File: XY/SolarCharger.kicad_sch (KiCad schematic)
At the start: 42 parts, among them U13 ADM1176-1ARMZ-R7

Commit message: Updated layout
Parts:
- F6, F7, F8: footprint (none) -> Fuse:Fuse_0603_1608Metric
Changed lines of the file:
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@@
 			)
 		)
-		(property "Footprint" ""
+		(property "Footprint" "Fuse:Fuse_0603_1608Metric"
 			(at 41.91 153.67 0)
 			(effects
@@
 			)
 		)
-		(property "Footprint" ""
+		(property "Footprint" "Fuse:Fuse_0603_1608Metric"
 			(at 41.91 109.22 0)
 			(effects
@@
 			)
 		)
-		(property "Footprint" ""
+		(property "Footprint" "Fuse:Fuse_0603_1608Metric"
 			(at 123.19 31.75 0)
 			(effects

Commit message: almost done
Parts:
- added SC6: SM141K06TF, Argus-Miscellaneous:SM141K06TF, symbol Device:Solar_Cell
- SC1, SC2, SC4, SC5: footprint SolarPanels:SM141K06TF -> Argus-Miscellaneous:SM141K06TF
- SC3: footprint SolarPanels:SM141K10TF -> Argus-Miscellaneous:SM141K10TF
- U13: symbol Mainboard:ADM1176-1ARMZ-R7 -> Argus-IC:ADM1176-1ARMZ-R7
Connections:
- net at D3.1 (K), D4.2 (A), SC3.1 (+)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: now also SC6.1 (+)
- net at D2.1 (K), D3.2 (A), SC2.1 (+)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: now also SC6.2 (-)
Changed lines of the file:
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@@
 	(wire
 		(pts
+			(xy 90.17 39.37) (xy 92.71 39.37)
+		)
+		(stroke
+			(width 0)
+			(type default)
+		)
+	)
+	(wire
+		(pts
 			(xy 99.06 91.44) (xy 105.41 91.44)
 		)
@@
 	(wire
 		(pts
+			(xy 82.55 39.37) (xy 80.01 39.37)
+		)
+		(stroke
+			(width 0)
+			(type default)
+		)
+	)
+	(wire
+		(pts
 			(xy 105.41 168.91) (xy 111.76 168.91)
 		)
@@
 	(wire
 		(pts
+			(xy 80.01 39.37) (xy 80.01 31.75)
+		)
+		(stroke
+			(width 0)
+			(type default)
+		)
+	)
+	(wire
+		(pts
 			(xy 62.23 123.19) (xy 62.23 124.46)
 		)
@@
 	(wire
 		(pts
+			(xy 92.71 39.37) (xy 92.71 31.75)
+		)
+		(stroke
+			(width 0)
+			(type default)
+		)
+	)
+	(wire
+		(pts
 			(xy 212.09 81.28) (xy 217.17 81.28)
 		)
@@
 			)
 		)
-		(property "Footprint" "SolarPanels:SM141K06TF"
+		(property "Footprint" "Argus-Miscellaneous:SM141K06TF"
 			(at 99.314 31.75 90)
 			(effects
@@
 	)
 	(symbol
-		(lib_id "Mainboard:ADM1176-1ARMZ-R7")
+		(lib_id "Argus-IC:ADM1176-1ARMZ-R7")
 		(at 233.68 81.28 0)
 		(unit 1)
@@
 	)
 	(symbol
+		(lib_id "Device:Solar_Cell")
+		(at 85.09 39.37 270)
+		(unit 1)
+		(exclude_from_sim no)
+		(in_bom yes)
+		(on_board yes)
+		(dnp yes)
+		(property "Reference" "SC6"
+			(at 86.614 43.18 90)
+			(effects
+				(font
+					(size 1.27 1.27)
+				)
+			)
+		)
+		(property "Value" "SM141K06TF"
+			(at 86.868 45.212 90)
+			(effects
+				(font
+					(size 1.27 1.27)
+				)
+			)
+		)
+		(property "Footprint" "Argus-Miscellaneous:SM141K06TF"
+			(at 86.614 39.37 90)
+			(effects
+				(font
+					(size 1.27 1.27)
+				)
+				(hide yes)
+			)
+		)
+		(property "Datasheet" "~"
+			(at 86.614 39.37 90)
+			(effects
+				(font
+					(size 1.27 1.27)
+				)
+				(hide yes)
+			)
+		)
+		(property "Description" "Single solar cell"
+			(at 85.09 39.37 0)
+			(effects
+				(font
+					(size 1.27 1.27)
+				)
+				(hide yes)
+			)
+		)
+		(pin "2"
+		)
+		(pin "1"
+		)
+		(instances
+			(project "Avionics-SolarPanels"
+				(path "/92e58b76-9357-4452-b231-18fffdf58e73/bef00a2e-eb3a-4ecf-812a-1c3ccf6e8d66"
+					(reference "SC6")
+					(unit 1)
+				)
+			)
+		)
+	)
+	(symbol
 		(lib_id "Device:R_Small")
 		(at 111.76 68.58 0)
@@
 			)
 		)
-		(property "Footprint" "SolarPanels:SM141K06TF"
+		(property "Footprint" "Argus-Miscellaneous:SM141K06TF"
 			(at 112.014 31.75 90)
 			(effects
@@
 			)
 		)
-		(property "Footprint" "SolarPanels:SM141K06TF"
+		(property "Footprint" "Argus-Miscellaneous:SM141K06TF"
 			(at 61.214 31.75 90)
 			(effects
@@
 			)
 		)
-		(property "Footprint" "SolarPanels:SM141K06TF"
+		(property "Footprint" "Argus-Miscellaneous:SM141K06TF"
 			(at 73.914 31.75 90)
 			(effects
@@
 			)
 		)
-		(property "Footprint" "SolarPanels:SM141K10TF"
+		(property "Footprint" "Argus-Miscellaneous:SM141K10TF"
 			(at 86.614 31.75 90)
 			(effects

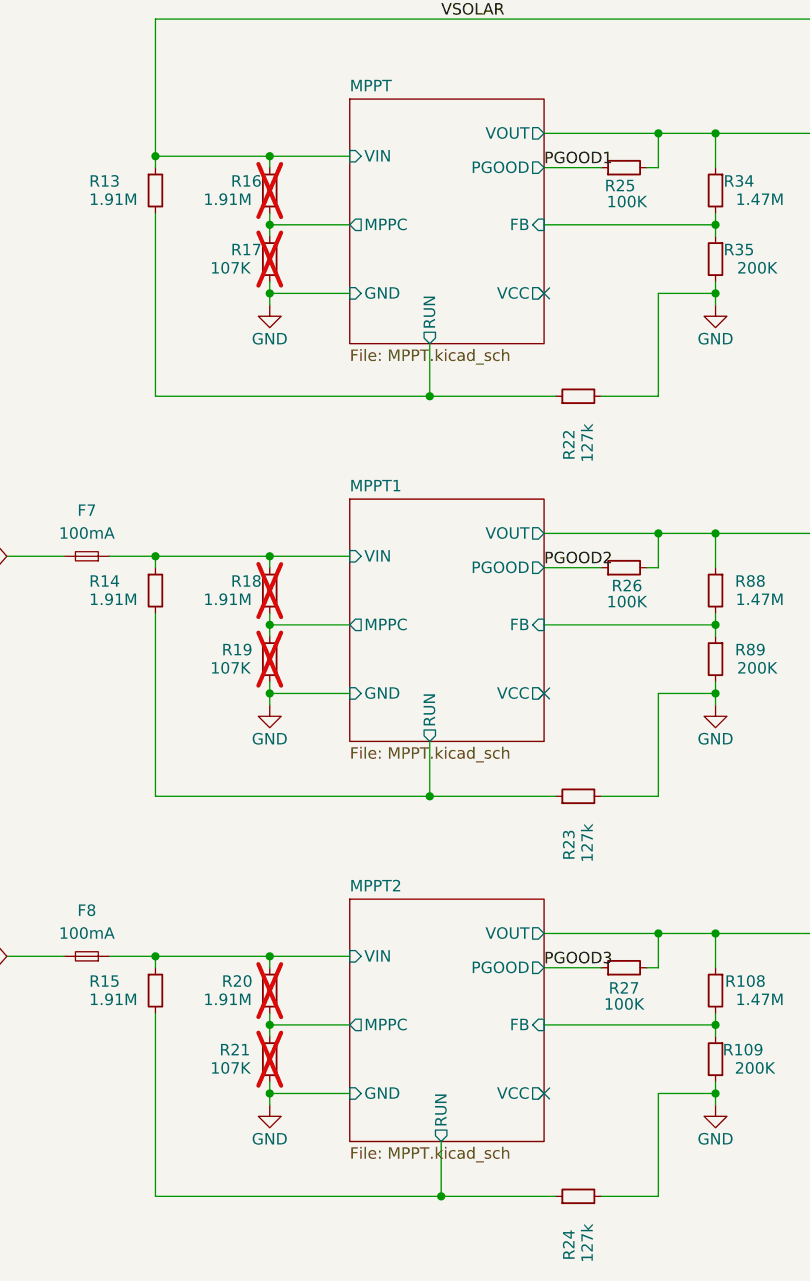
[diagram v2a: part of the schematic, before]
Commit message: Increased usbc connnector size
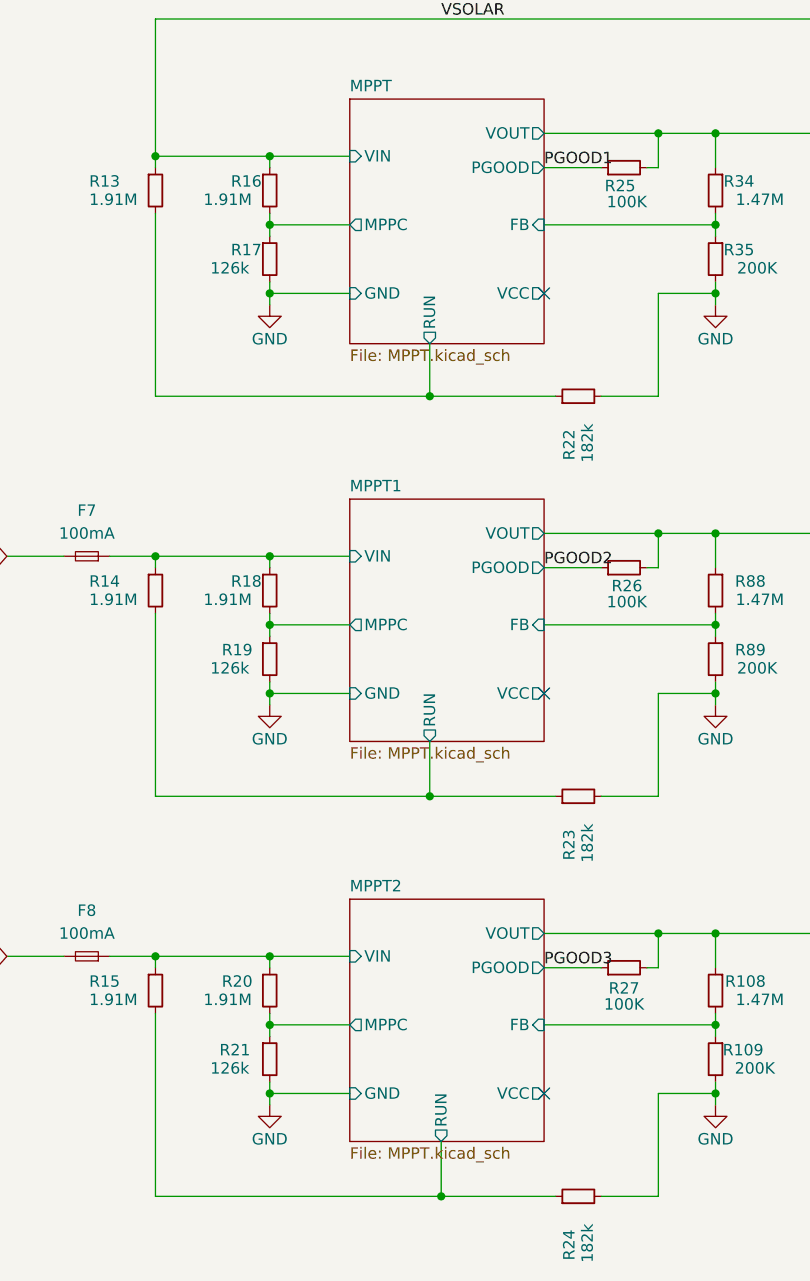
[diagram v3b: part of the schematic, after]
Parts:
- R16, R18, R20: now fitted
- R17, R19, R21: value 107K -> 126k; now fitted
- R22, R23, R24: value 127k -> 182k
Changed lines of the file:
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@@
 		(in_bom yes)
 		(on_board yes)
-		(dnp yes)
+		(dnp no)
 		(property "Reference" "R16"
 			(at 57.912 67.564 0)
@@
 		(in_bom yes)
 		(on_board yes)
-		(dnp yes)
+		(dnp no)
 		(property "Reference" "R20"
 			(at 56.896 156.464 0)
@@
 		(in_bom yes)
 		(on_board yes)
-		(dnp yes)
+		(dnp no)
 		(property "Reference" "R21"
 			(at 56.642 164.084 0)
@@
 			)
 		)
-		(property "Value" "107K"
+		(property "Value" "126k"
 			(at 55.626 166.116 0)
 			(effects
@@
 			)
 		)
-		(property "Value" "127k"
+		(property "Value" "182k"
 			(at 97.536 187.706 0)
 			(effects
@@
 			)
 		)
-		(property "Value" "127k"
+		(property "Value" "182k"
 			(at 97.536 98.806 0)
 			(effects
@@
 		(in_bom yes)
 		(on_board yes)
-		(dnp yes)
+		(dnp no)
 		(property "Reference" "R18"
 			(at 57.912 112.014 0)
@@
 		(in_bom yes)
 		(on_board yes)
-		(dnp yes)
+		(dnp no)
 		(property "Reference" "R19"
 			(at 56.896 119.634 0)
@@
 			)
 		)
-		(property "Value" "107K"
+		(property "Value" "126k"
 			(at 55.626 121.666 0)
 			(effects
@@
 			)
 		)
-		(property "Value" "127k"
+		(property "Value" "182k"
 			(at 97.536 143.256 0)
 			(effects
@@
 		(in_bom yes)
 		(on_board yes)
-		(dnp yes)
+		(dnp no)
 		(property "Reference" "R17"
 			(at 57.912 75.184 0)
@@
 			)
 		)
-		(property "Value" "107K"
+		(property "Value" "126k"
 			(at 55.626 77.216 0)
 			(effects

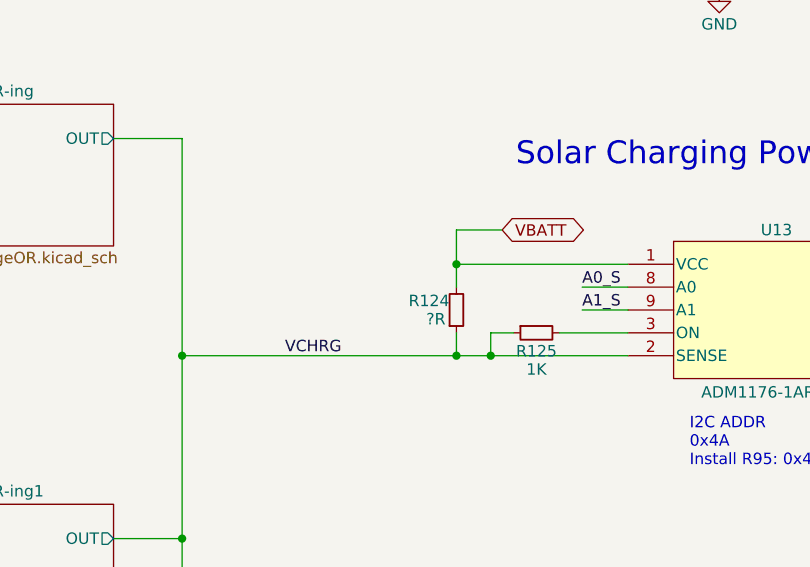
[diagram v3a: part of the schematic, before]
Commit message: Added fusing to power monitor
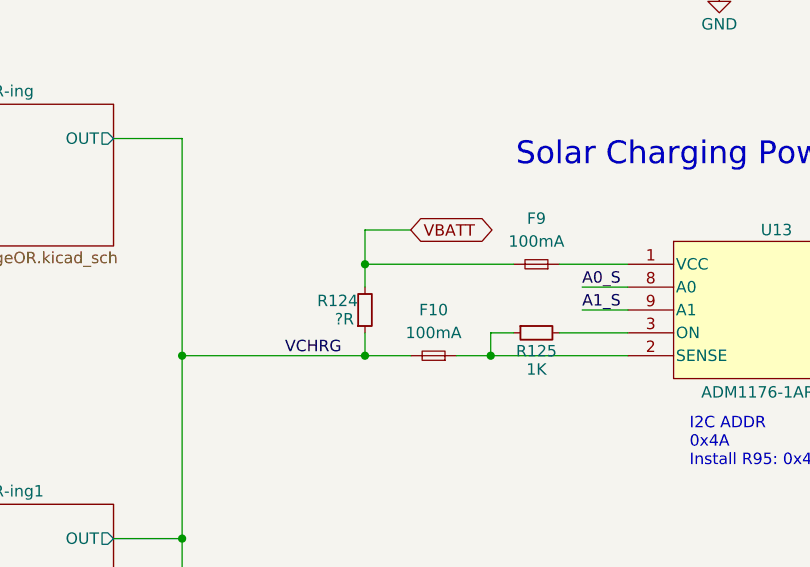
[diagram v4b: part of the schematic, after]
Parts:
- added F10, F9: 100mA, Fuse:Fuse_0603_1608Metric, symbol Device:Fuse_Small
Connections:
- net VBATT: now also F9.2; no longer U13.1 (VCC)
- net VCHRG: now also F10.2; no longer R125.1, U13.2 (SENSE)
- new net: F9.1, U13.1 (VCC)
- new net: F10.1, R125.1, U13.2 (SENSE)
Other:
- moved on the sheet: R124
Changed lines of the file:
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@@
 	)
 	(junction
-		(at 198.12 76.2)
-		(diameter 0)
-		(color 0 0 0 0)
-	)
-	(junction
 		(at 111.76 168.91)
 		(diameter 0)
@@
 	)
 	(junction
+		(at 201.93 86.36)
+		(diameter 0)
+		(color 0 0 0 0)
+	)
+	(junction
 		(at 227.33 35.56)
 		(diameter 0)
@@
 	)
 	(junction
+		(at 187.96 76.2)
+		(diameter 0)
+		(color 0 0 0 0)
+	)
+	(junction
 		(at 80.01 31.75)
 		(diameter 0)
@@
 	)
 	(junction
-		(at 198.12 86.36)
-		(diameter 0)
-		(color 0 0 0 0)
-	)
-	(junction
 		(at 67.31 31.75)
 		(diameter 0)
@@
 	)
 	(junction
-		(at 201.93 86.36)
-		(diameter 0)
-		(color 0 0 0 0)
-	)
-	(junction
 		(at 62.23 80.01)
 		(diameter 0)
@@
 	)
 	(junction
+		(at 187.96 86.36)
+		(diameter 0)
+		(color 0 0 0 0)
+	)
+	(junction
 		(at 105.41 31.75)
 		(diameter 0)
@@
 	(wire
 		(pts
-			(xy 198.12 76.2) (xy 198.12 72.39)
+			(xy 187.96 72.39) (xy 187.96 76.2)
 		)
 		(stroke
@@
 	(wire
 		(pts
-			(xy 114.3 25.4) (xy 118.11 25.4)
+			(xy 187.96 76.2) (xy 204.47 76.2)
 		)
 		(stroke
@@
 	(wire
 		(pts
-			(xy 242.57 146.05) (xy 261.62 146.05)
+			(xy 114.3 25.4) (xy 118.11 25.4)
 		)
 		(stroke
@@
 	(wire
 		(pts
-			(xy 198.12 76.2) (xy 198.12 78.74)
+			(xy 242.57 146.05) (xy 261.62 146.05)
 		)
 		(stroke
@@
 	(wire
 		(pts
+			(xy 187.96 86.36) (xy 193.04 86.36)
+		)
+		(stroke
+			(width 0)
+			(type default)
+		)
+	)
+	(wire
+		(pts
 			(xy 49.53 153.67) (xy 49.53 154.94)
 		)
@@
 	(wire
 		(pts
-			(xy 105.41 151.13) (xy 105.41 154.94)
+			(xy 187.96 76.2) (xy 187.96 78.74)
 		)
 		(stroke
@@
 	(wire
 		(pts
-			(xy 80.01 31.75) (xy 80.01 25.4)
+			(xy 105.41 151.13) (xy 105.41 154.94)
 		)
 		(stroke
@@
 	(wire
 		(pts
-			(xy 242.57 35.56) (xy 245.11 35.56)
+			(xy 80.01 31.75) (xy 80.01 25.4)
 		)
 		(stroke
@@
 	(wire
 		(pts
-			(xy 99.06 135.89) (xy 105.41 135.89)
+			(xy 242.57 35.56) (xy 245.11 35.56)
 		)
 		(stroke
@@
 	(wire
 		(pts
-			(xy 82.55 39.37) (xy 80.01 39.37)
+			(xy 99.06 135.89) (xy 105.41 135.89)
 		)
 		(stroke
@@
 	(wire
 		(pts
-			(xy 105.41 168.91) (xy 111.76 168.91)
+			(xy 82.55 39.37) (xy 80.01 39.37)
 		)
 		(stroke
@@
 	(wire
 		(pts
-			(xy 198.12 86.36) (xy 201.93 86.36)
+			(xy 105.41 168.91) (xy 111.76 168.91)
 		)
 		(stroke
@@
 	(wire
 		(pts
-			(xy 203.2 72.39) (xy 198.12 72.39)
+			(xy 193.04 72.39) (xy 187.96 72.39)
 		)
 		(stroke
@@
 	(wire
 		(pts
-			(xy 167.64 86.36) (xy 198.12 86.36)
+			(xy 167.64 86.36) (xy 187.96 86.36)
 		)
 		(stroke
@@
 	(wire
 		(pts
+			(xy 209.55 76.2) (xy 217.17 76.2)
+		)
+		(stroke
+			(width 0)
+			(type default)
+		)
+	)
+	(wire
+		(pts
 			(xy 67.31 25.4) (xy 71.12 25.4)
 		)
@@
 	(wire
 		(pts
-			(xy 198.12 83.82) (xy 198.12 86.36)
+			(xy 187.96 83.82) (xy 187.96 86.36)
+		)
+		(stroke
+			(width 0)
+			(type default)
+		)
+	)
+	(wire
+		(pts
+			(xy 198.12 86.36) (xy 201.93 86.36)
 		)
 		(stroke
@@
 	(wire
 		(pts
-			(xy 198.12 76.2) (xy 217.17 76.2)
-		)
-		(stroke
-			(width 0)
-			(type default)
-		)
-	)
-	(wire
-		(pts
 			(xy 111.76 168.91) (xy 111.76 170.18)
 		)
@@
 	(global_label "VBATT"
 		(shape bidirectional)
-		(at 203.2 72.39 0)
+		(at 193.04 72.39 0)
 		(effects
 			(font
@@
 		)
 		(property "Intersheetrefs" "${INTERSHEET_REFS}"
-			(at 203.2 72.39 0)
+			(at 193.04 72.39 0)
 			(effects
 				(font
@@
 	)
 	(symbol
+		(lib_id "Device:Fuse_Small")
+		(at 207.01 76.2 180)
+		(unit 1)
+		(exclude_from_sim no)
+		(in_bom yes)
+		(on_board yes)
+		(dnp no)
+		(fields_autoplaced yes)
+		(property "Reference" "F9"
+			(at 207.01 71.12 0)
+			(effects
+				(font
+					(size 1.27 1.27)
+				)
+			)
+		)
+		(property "Value" "100mA"
+			(at 207.01 73.66 0)
+			(effects
+				(font
+					(size 1.27 1.27)
+				)
+			)
+		)
+		(property "Footprint" "Fuse:Fuse_0603_1608Metric"
+			(at 207.01 76.2 0)
+			(effects
+				(font
+					(size 1.27 1.27)
+				)
+				(hide yes)
+			)
+		)
+		(property "Datasheet" "~"
+			(at 207.01 76.2 0)
+			(effects
+				(font
+					(size 1.27 1.27)
+				)
+				(hide yes)
+			)
+		)
+		(property "Description" "Fuse, small symbol"
+			(at 207.01 76.2 0)
+			(effects
+				(font
+					(size 1.27 1.27)
+				)
+				(hide yes)
+			)
+		)
+		(pin "2"
+		)
+		(pin "1"
+		)
+		(instances
+			(project "Avionics-SolarPanels"
+				(path "/92e58b76-9357-4452-b231-18fffdf58e73/bef00a2e-eb3a-4ecf-812a-1c3ccf6e8d66"
+					(reference "F9")
+					(unit 1)
+				)
+			)
+		)
+	)
+	(symbol
 		(lib_id "Device:C_Small")
 		(at 260.35 76.2 270)
@@
 	)
 	(symbol
+		(lib_id "Device:Fuse_Small")
+		(at 195.58 86.36 180)
+		(unit 1)
+		(exclude_from_sim no)
+		(in_bom yes)
+		(on_board yes)
+		(dnp no)
+		(fields_autoplaced yes)
+		(property "Reference" "F10"
+			(at 195.58 81.28 0)
+			(effects
+				(font
+					(size 1.27 1.27)
+				)
+			)
+		)
+		(property "Value" "100mA"
+			(at 195.58 83.82 0)
+			(effects
+				(font
+					(size 1.27 1.27)
+				)
+			)
+		)
+		(property "Footprint" "Fuse:Fuse_0603_1608Metric"
+			(at 195.58 86.36 0)
+			(effects
+				(font
+					(size 1.27 1.27)
+				)
+				(hide yes)
+			)
+		)
+		(property "Datasheet" "~"
+			(at 195.58 86.36 0)
+			(effects
+				(font
+					(size 1.27 1.27)
+				)
+				(hide yes)
+			)
+		)
+		(property "Description" "Fuse, small symbol"
+			(at 195.58 86.36 0)
+			(effects
+				(font
+					(size 1.27 1.27)
+				)
+				(hide yes)
+			)
+		)
+		(pin "2"
+		)
+		(pin "1"
+		)
+		(instances
+			(project "Avionics-SolarPanels"
+				(path "/92e58b76-9357-4452-b231-18fffdf58e73/bef00a2e-eb3a-4ecf-812a-1c3ccf6e8d66"
+					(reference "F10")
+					(unit 1)
+				)
+			)
+		)
+	)
+	(symbol
 		(lib_id "Device:R_Small")
 		(at 111.76 165.1 0)
@@
 	(symbol
 		(lib_id "Device:R_Small")
-		(at 198.12 81.28 0)
+		(at 187.96 81.28 0)
 		(mirror x)
 		(unit 1)
@@
 		(dnp no)
 		(property "Reference" "R124"
-			(at 195.072 80.264 0)
+			(at 184.912 80.264 0)
 			(effects
 				(font
@@
 		)
 		(property "Value" "?R"
-			(at 195.834 82.296 0)
+			(at 185.674 82.296 0)
 			(effects
 				(font
@@
 		)
 		(property "Footprint" "Resistor_SMD:R_2512_6332Metric"
-			(at 198.12 81.28 0)
+			(at 187.96 81.28 0)
 			(effects
 				(font
@@
 		)
 		(property "Datasheet" "~"
-			(at 198.12 81.28 0)
+			(at 187.96 81.28 0)
 			(effects
 				(font
@@
 		)
 		(property "Description" "Resistor, small symbol"
-			(at 198.12 81.28 0)
+			(at 187.96 81.28 0)
 			(effects
 				(font

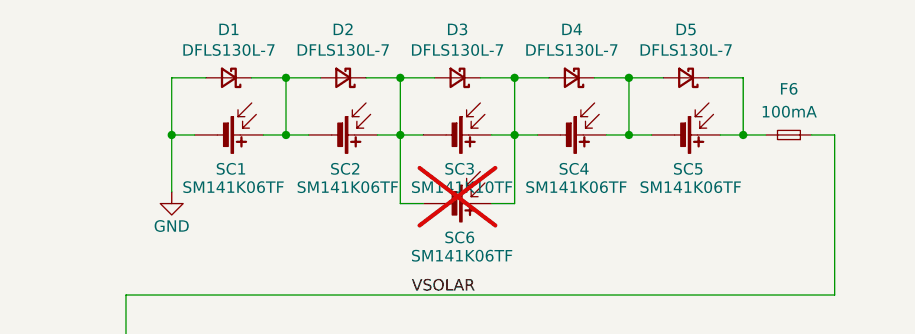
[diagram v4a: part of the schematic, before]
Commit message: Updated silkscreen and part number for solar panel bypass
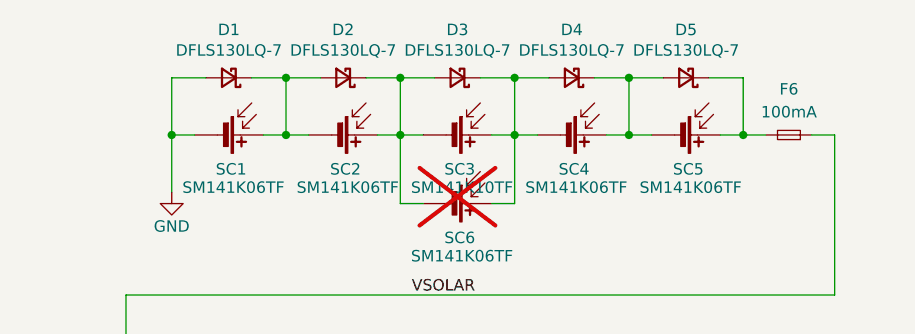
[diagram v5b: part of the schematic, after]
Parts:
- D1, D2, D3, D4, D5: value DFLS130L-7 -> DFLS130LQ-7
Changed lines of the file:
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@@
 			)
 		)
-		(property "Value" "DFLS130L-7"
+		(property "Value" "DFLS130LQ-7"
 			(at 86.36 22.352 0)
 			(effects
@@
 			)
 		)
-		(property "Value" "DFLS130L-7"
+		(property "Value" "DFLS130LQ-7"
 			(at 73.66 22.352 0)
 			(effects
@@
 			)
 		)
-		(property "Value" "DFLS130L-7"
+		(property "Value" "DFLS130LQ-7"
 			(at 99.06 22.352 0)
 			(effects
@@
 			)
 		)
-		(property "Value" "DFLS130L-7"
+		(property "Value" "DFLS130LQ-7"
 			(at 60.96 22.352 0)
 			(effects
@@
 			)
 		)
-		(property "Value" "DFLS130L-7"
+		(property "Value" "DFLS130LQ-7"
 			(at 111.76 22.352 0)
 			(effects
